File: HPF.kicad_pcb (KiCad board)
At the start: 4 copper layers, 100 x 100 mm, 723 parts, among them J1 CONN_COAXIAL, J2 Conn_01x12, J3 CONN_COAXIAL, J4 CONN_COAXIAL, J5 CONN_COAXIAL, Q2 zvp2106G, U1 AP1117-50, U2 PGA103+

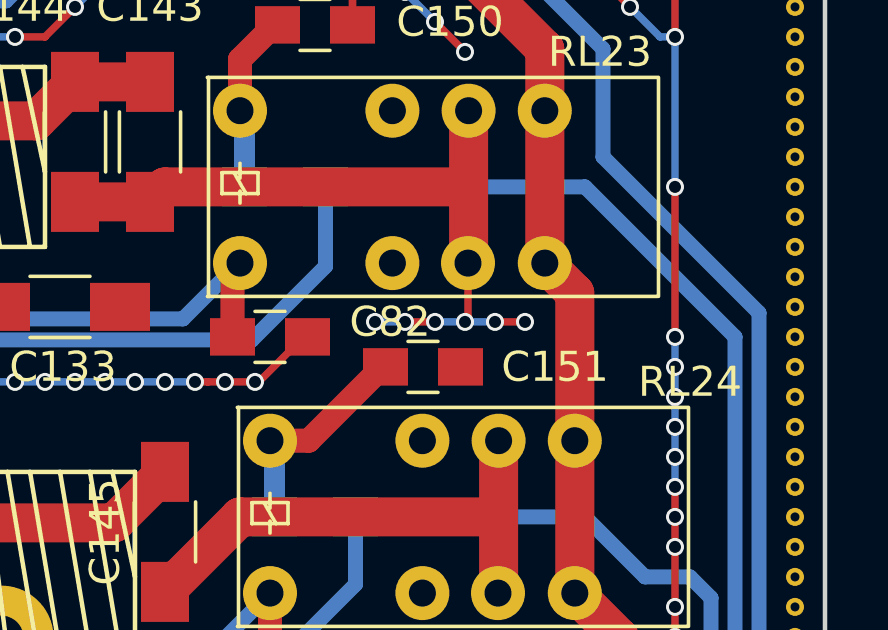
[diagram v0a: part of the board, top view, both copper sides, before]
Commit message: minor stiching error gone, new inductance spreadsheet
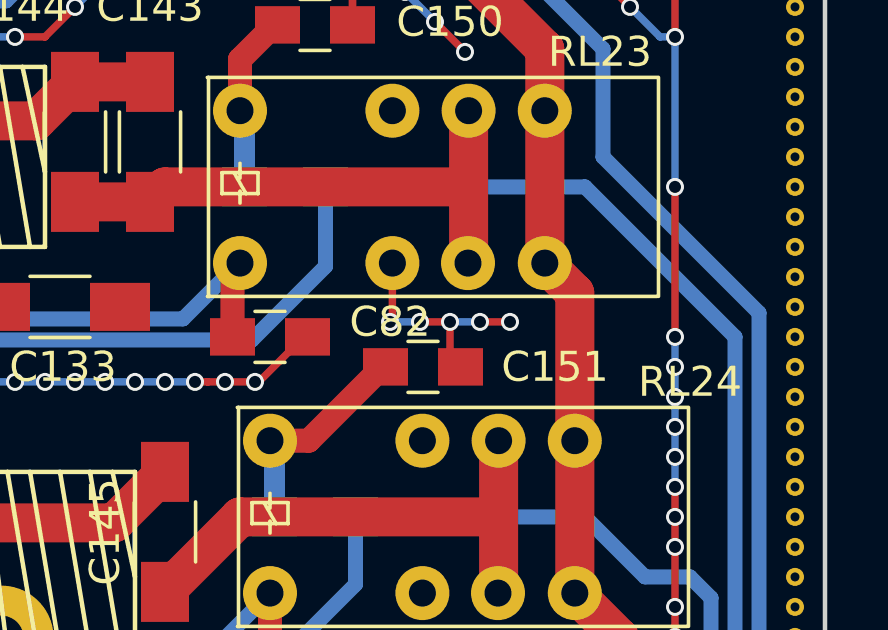
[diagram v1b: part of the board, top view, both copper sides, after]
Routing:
- net GND: track 936.7 -> 944.3 mm, vias 609 -> 614
- net Net-(C143-Pad1): track 25.4 -> 18.4 mm, vias 6 -> 0
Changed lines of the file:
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@@
   (page A4)
   (layers
-    (0 F.Cu signal)
+    (0 F.Cu signal hide)
     (1 In1.Cu signal hide)
     (2 In2.Cu signal hide)
@@
   (segment (start 98.6 84.8) (end 106 84.8) (width 0.8) (layer B.Cu) (net 1))
   (segment (start 134 91.8) (end 168.24 91.8) (width 0.8) (layer B.Cu) (net 1))
+  (segment (start 177.5 34.5) (end 177.5 35.65) (width 0.25) (layer F.Cu) (net 2))
+  (segment (start 177.5 35.65) (end 177.85 36) (width 0.25) (layer F.Cu) (net 2))
+  (segment (start 175.58 32.54) (end 175.58 34.42) (width 0.25) (layer F.Cu) (net 2))
+  (via (at 179.5 34.5) (size 0.6) (drill 0.4) (layers F.Cu B.Cu) (net 2))
+  (segment (start 178.5 34.5) (end 179.5 34.5) (width 0.25) (layer F.Cu) (net 2))
+  (via (at 178.5 34.5) (size 0.6) (drill 0.4) (layers F.Cu B.Cu) (net 2))
+  (segment (start 177.5 34.5) (end 178.5 34.5) (width 0.25) (layer B.Cu) (net 2))
+  (via (at 177.5 34.5) (size 0.6) (drill 0.4) (layers F.Cu B.Cu) (net 2))
+  (segment (start 176.5 34.5) (end 177.5 34.5) (width 0.25) (layer F.Cu) (net 2))
+  (via (at 176.5 34.5) (size 0.6) (drill 0.4) (layers F.Cu B.Cu) (net 2))
+  (segment (start 175.5 34.5) (end 176.5 34.5) (width 0.25) (layer B.Cu) (net 2))
+  (via (at 175.5 34.5) (size 0.6) (drill 0.4) (layers F.Cu B.Cu) (net 2))
+  (segment (start 175.58 34.42) (end 175.5 34.5) (width 0.25) (layer F.Cu) (net 2))
   (via (at 99 78) (size 0.6) (drill 0.4) (layers F.Cu B.Cu) (net 2))
   (via (at 99 77) (size 0.6) (drill 0.4) (layers F.Cu B.Cu) (net 2))
@@
   (segment (start 162.54 76.54) (end 162.54 76.96) (width 1.3) (layer F.Cu) (net 36))
   (segment (start 162.54 76.96) (end 160 79.5) (width 1.3) (layer F.Cu) (net 36))
-  (segment (start 178 34.5) (end 177 34.5) (width 0.25) (layer B.Cu) (net 37))
-  (via (at 175 34.5) (size 0.6) (drill 0.4) (layers F.Cu B.Cu) (net 37))
-  (segment (start 176 34.5) (end 175 34.5) (width 0.25) (layer B.Cu) (net 37))
-  (via (at 176 34.5) (size 0.6) (drill 0.4) (layers F.Cu B.Cu) (net 37))
-  (segment (start 177 34.5) (end 176 34.5) (width 0.25) (layer F.Cu) (net 37))
-  (via (at 177 34.5) (size 0.6) (drill 0.4) (layers F.Cu B.Cu) (net 37))
-  (segment (start 178.1 32.54) (end 178.1 34.4) (width 0.25) (layer F.Cu) (net 37))
-  (via (at 180 34.5) (size 0.6) (drill 0.4) (layers F.Cu B.Cu) (net 37))
-  (segment (start 179 34.5) (end 180 34.5) (width 0.25) (layer F.Cu) (net 37))
-  (via (at 179 34.5) (size 0.6) (drill 0.4) (layers F.Cu B.Cu) (net 37))
-  (segment (start 178 34.5) (end 179 34.5) (width 0.25) (layer B.Cu) (net 37))
-  (via (at 178 34.5) (size 0.6) (drill 0.4) (layers F.Cu B.Cu) (net 37))
-  (segment (start 178.1 34.4) (end 178 34.5) (width 0.25) (layer F.Cu) (net 37))
   (segment (start 178.12 30) (end 168 30) (width 1.3) (layer F.Cu) (net 37))
   (segment (start 168 30) (end 167.5 30.5) (width 1.3) (layer F.Cu) (net 37))

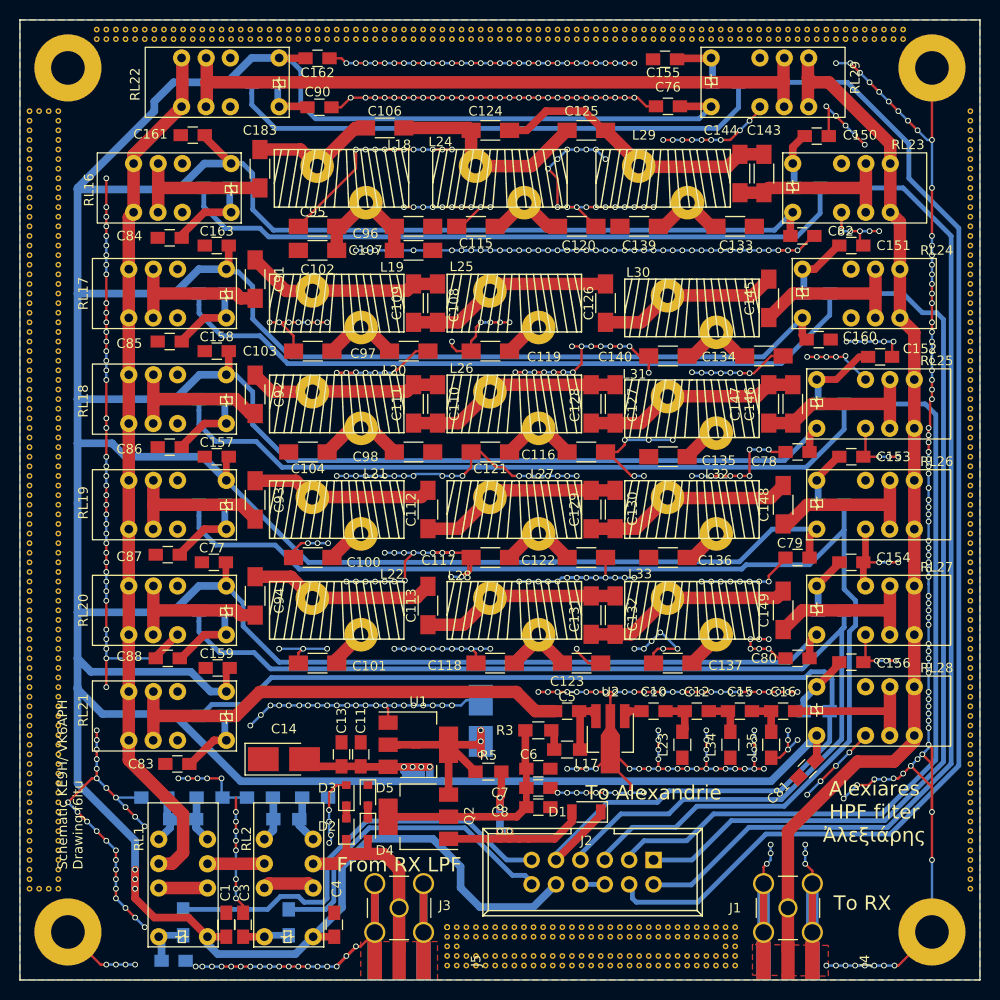
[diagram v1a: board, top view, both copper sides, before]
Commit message: upgrate to Kicad 5.0n, new up to date Gerber
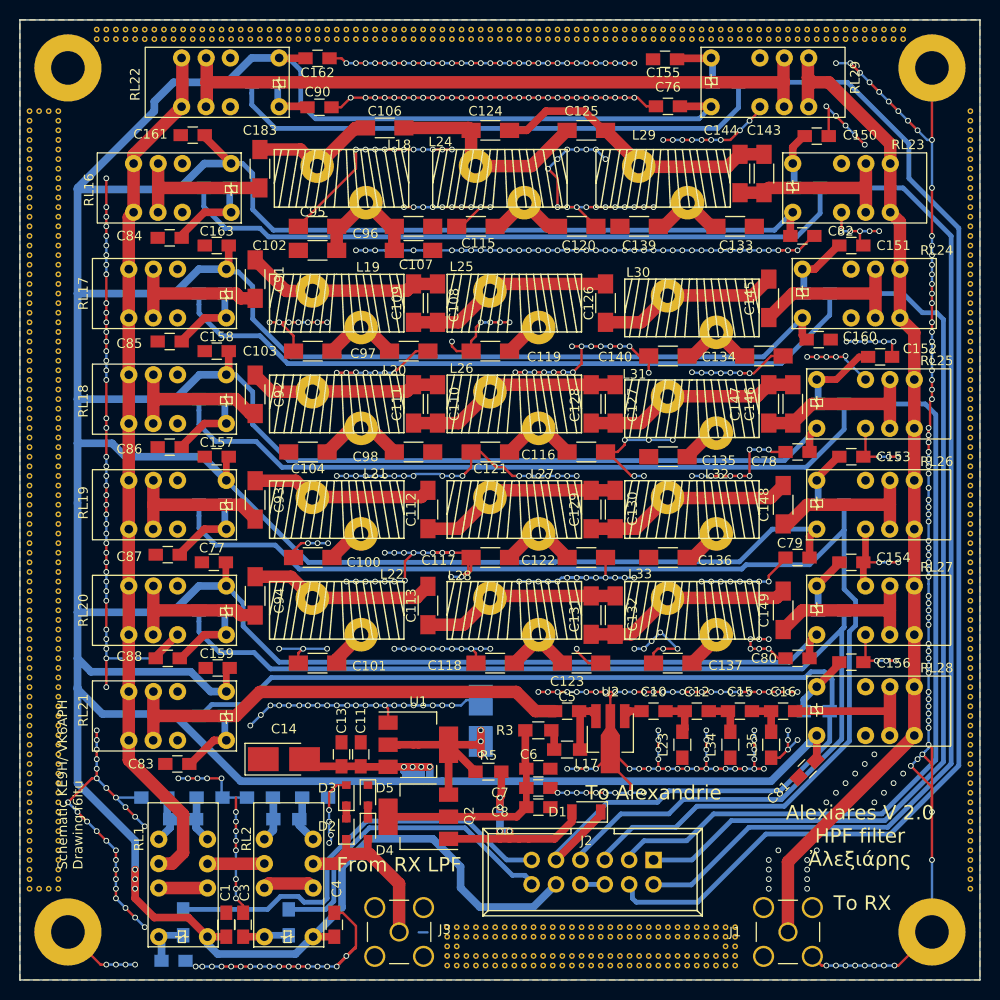
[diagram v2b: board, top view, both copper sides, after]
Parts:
- removed J4, J5: CONN_COAXIAL, SMA_PINS:SMA_EDGE_NRW
- moved J1 2.50 mm to (170.0, 107.5)
- moved J3 2.50 mm to (129.5, 107.5)
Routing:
- net GND: track 944.3 -> 858.0 mm, vias 614 -> 617
- net Net-(J1-Pad1): track 109.3 -> 105.1 mm
- net Net-(D2-Pad1): track 22.0 -> 18.9 mm
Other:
- board text added: "Alexiares V 2.0 HPF filter Ἀλεξιάρης"
- board text removed: "Alexiares HPF filter Ἀλεξιάρης"
